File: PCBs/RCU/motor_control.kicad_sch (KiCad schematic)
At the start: 18 parts, among them J300 Right_Encoder_Conn_01x04, J301 Right_Motor_Screw_Terminal_01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, J302 Left_Encoder_Conn_01x04, J303 Left_Motor_Screw_Terminal_01x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, U300 OPA365xxD, U301 DRV8876, U302 OPA365xxD, U303 DRV8876

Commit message: Corrected C302 and C305 values in motor drive units, should be 22nF, not 22uF
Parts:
- C302, C305: value 22uF -> (none)
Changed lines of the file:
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@@
       (effects (font (size 1.27 1.27)) (justify left))
     )
-    (property "Value" "22uF" (id 1) (at 180.34 63.5 0)
+    (property "Value" "" (id 1) (at 180.34 63.5 0)
       (effects (font (size 1.27 1.27)) (justify left))
     )
@@
       (effects (font (size 1.27 1.27)) (justify left))
     )
-    (property "Value" "22uF" (id 1) (at 179.07 118.11 0)
+    (property "Value" "" (id 1) (at 179.07 118.11 0)
       (effects (font (size 1.27 1.27)) (justify left))
     )

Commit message: Added 6V adjustable regulator to power motors and encoders
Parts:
- C302, C305: value (none) -> 22nF
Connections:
- net +9V is gone; now on net +6V: C300.1, C301.1, C303.1, C304.1, U301.11 (VM), U303.11 (VM)
- net +5V renamed +6V

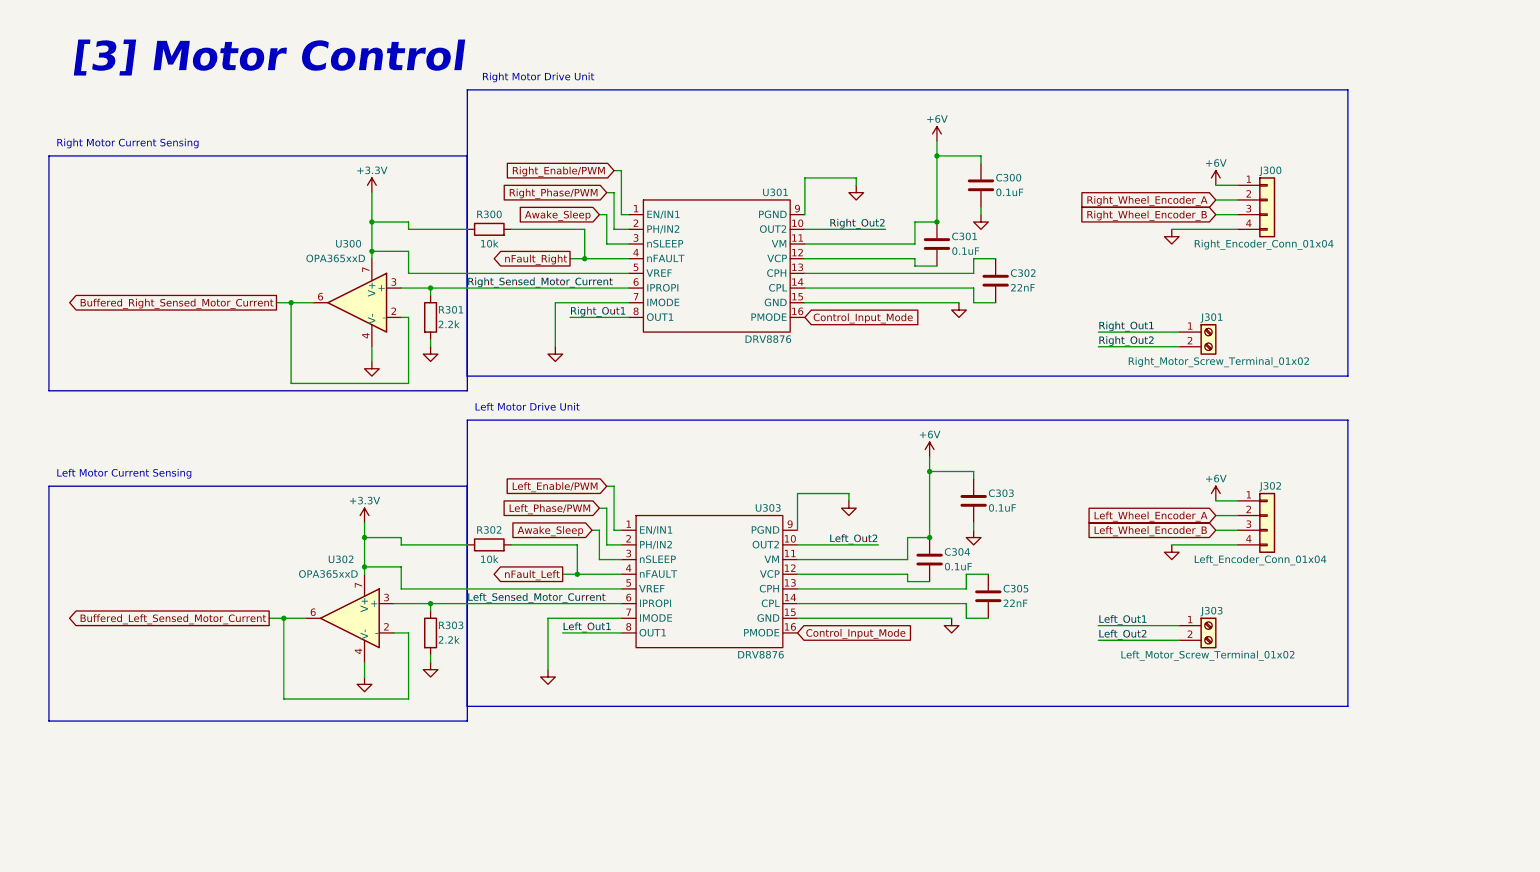
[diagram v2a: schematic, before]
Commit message: scaled down encoder output from 6V to 4V
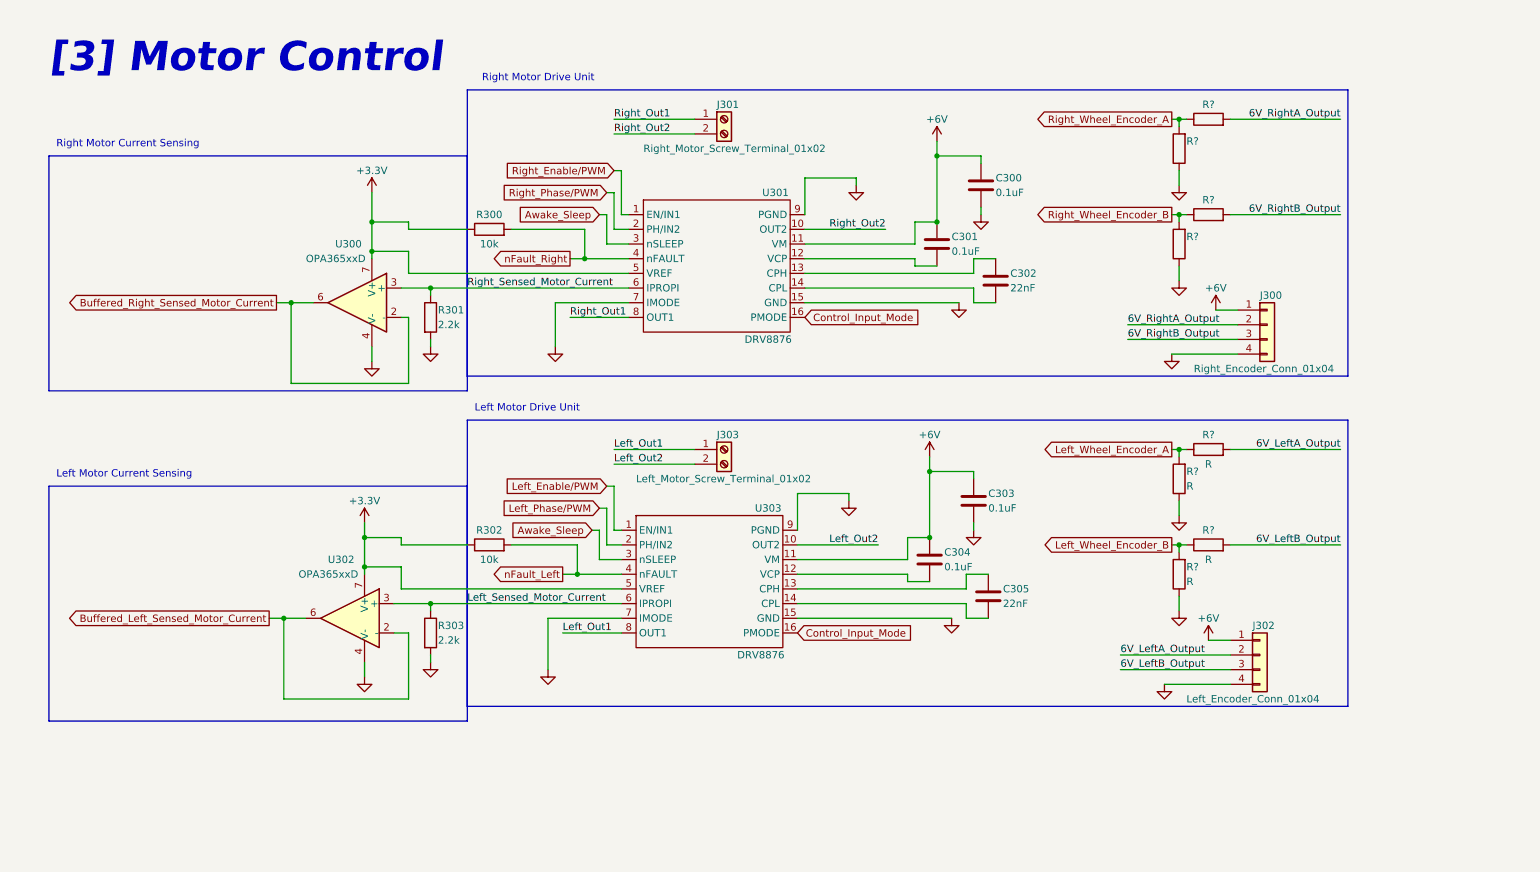
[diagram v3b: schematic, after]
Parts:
- added R? (x4): (no value), symbol Device:R
- added R? (x4): R, symbol Device:R
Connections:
- net GND: now also R?.1, R?.1, R?.1, R?.1
- net Left_Wheel_Encoder_A: now also R?.1, R?.2; no longer J302.2 (Pin_2)
- net Left_Wheel_Encoder_B: now also R?.1, R?.2; no longer J302.3 (Pin_3)
- net Right_Wheel_Encoder_A: now also R?.1, R?.2; no longer J300.2 (Pin_2)
- net Right_Wheel_Encoder_B: now also R?.1, R?.2; no longer J300.3 (Pin_3)
- new net 6V_LeftA_Output: J302.2 (Pin_2), R?.2
- new net 6V_LeftB_Output: J302.3 (Pin_3), R?.2
- new net 6V_RightA_Output: J300.2 (Pin_2), R?.2
- new net 6V_RightB_Output: J300.3 (Pin_3), R?.2
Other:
- moved on the sheet: J300, J301, J302, J303

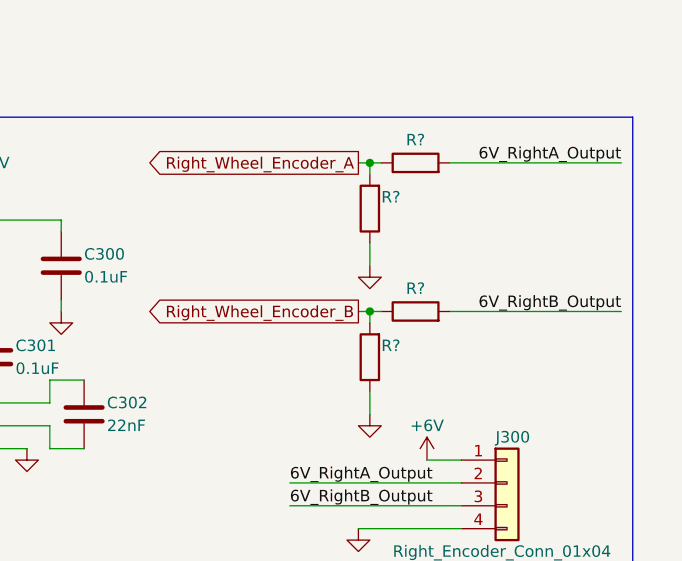
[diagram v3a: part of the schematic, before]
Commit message: Replaced Bidrectional TVS diodes with USBLC-2SC6 unidirectional ESD protection
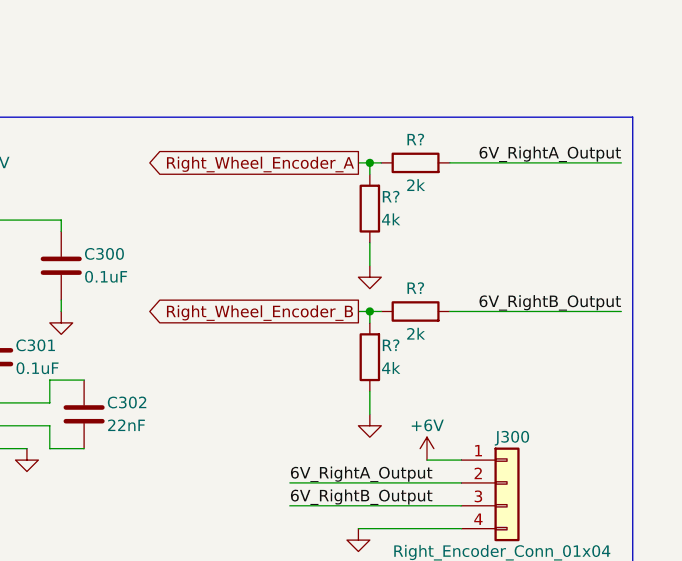
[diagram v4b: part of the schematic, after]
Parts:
- R? (x2): value (none) -> 4k
- R? (x2): value (none) -> 2k
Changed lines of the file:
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@@
       (effects (font (size 1.27 1.27)) (justify right))
     )
-    (property "Value" "" (id 1) (at 210.82 57.15 0)
+    (property "Value" "4k" (id 1) (at 210.82 57.15 0)
       (effects (font (size 1.27 1.27)) (justify right))
     )
@@
       (effects (font (size 1.27 1.27)) (justify right))
     )
-    (property "Value" "" (id 1) (at 210.82 40.64 0)
+    (property "Value" "4k" (id 1) (at 210.82 40.64 0)
       (effects (font (size 1.27 1.27)) (justify right))
     )
@@
     (in_bom yes) (on_board yes)
     (property "Reference" "R?" (id 0) (at 214.63 48.26 90))
-    (property "Value" "" (id 1) (at 214.63 53.34 90))
+    (property "Value" "2k" (id 1) (at 214.63 53.34 90))
     (property "Footprint" "" (id 2) (at 214.63 52.578 90)
       (effects (font (size 1.27 1.27)) hide)
@@
     (in_bom yes) (on_board yes)
     (property "Reference" "R?" (id 0) (at 214.63 31.75 90))
-    (property "Value" "" (id 1) (at 214.63 36.83 90))
+    (property "Value" "2k" (id 1) (at 214.63 36.83 90))
     (property "Footprint" "" (id 2) (at 214.63 36.068 90)
       (effects (font (size 1.27 1.27)) hide)

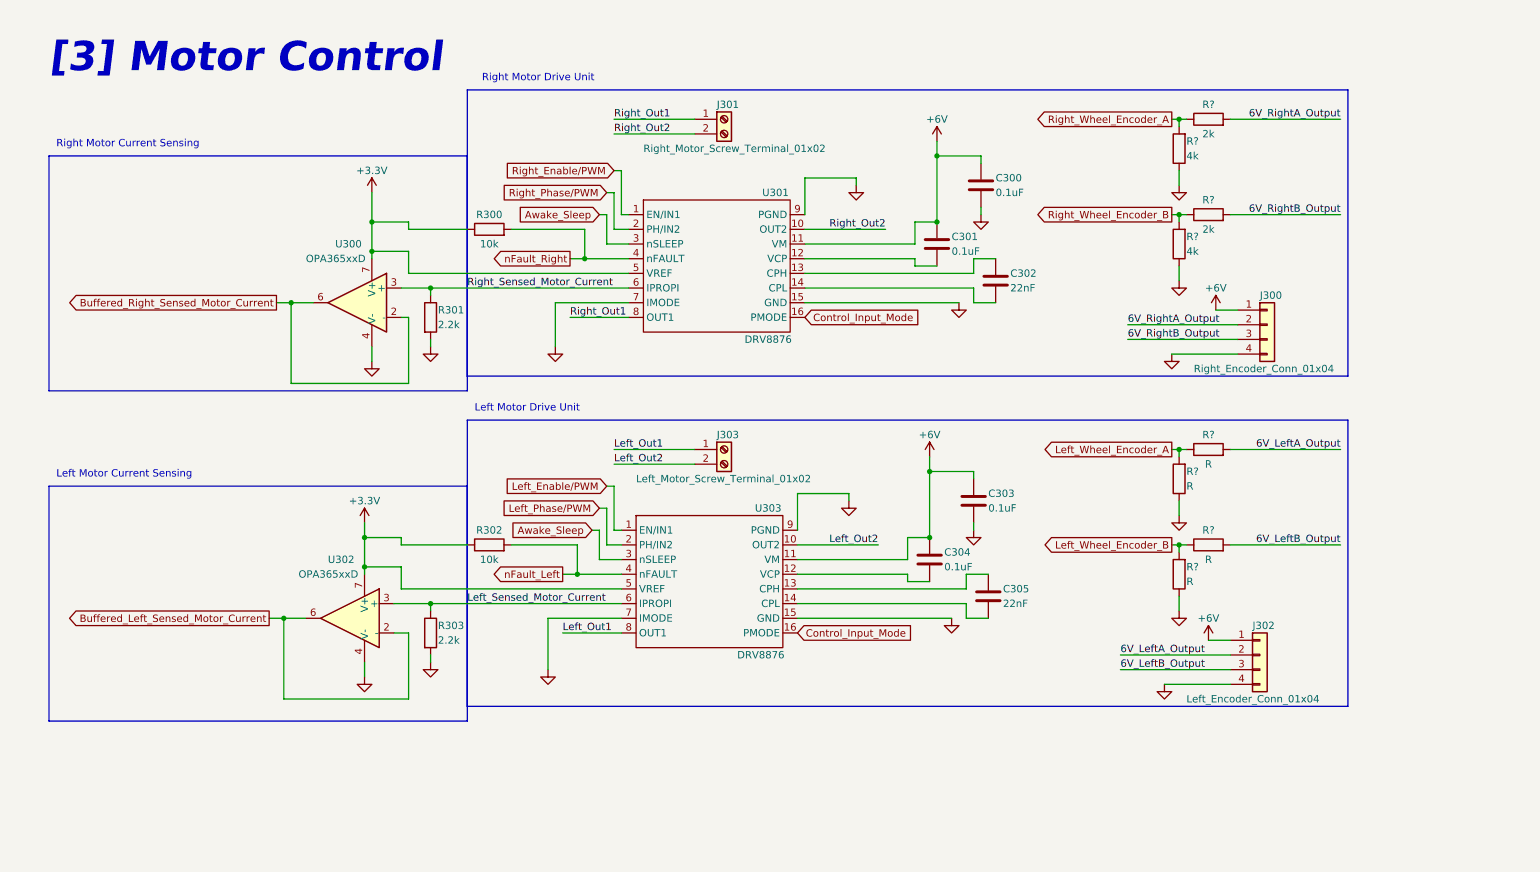
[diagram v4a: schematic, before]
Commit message: Added ESD protection to 3.3V pin of SWD connector, and made motor sheet larger
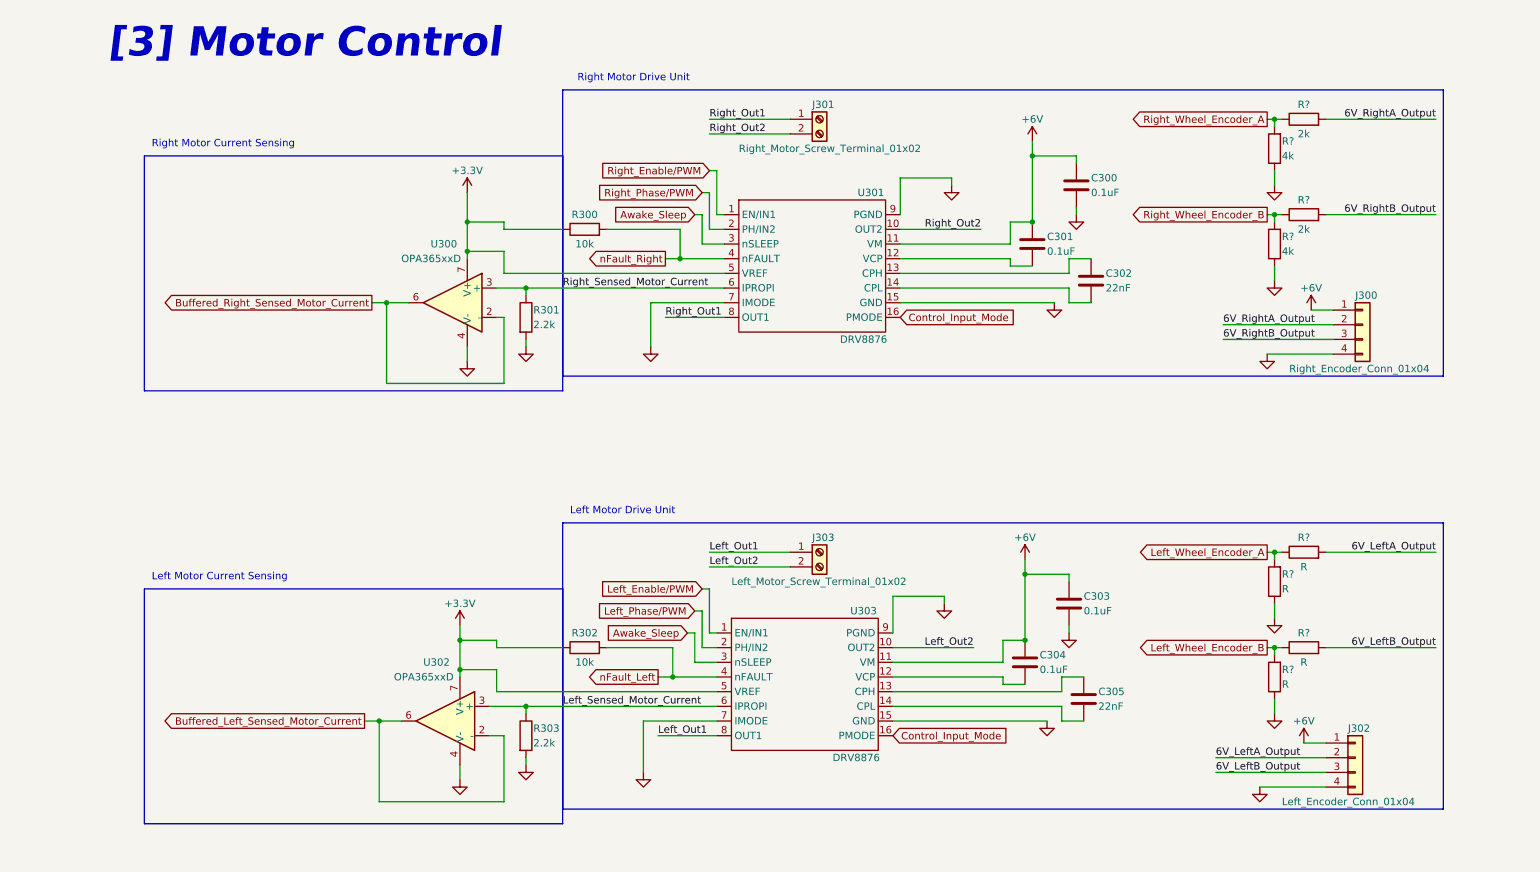
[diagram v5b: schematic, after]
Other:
- moved on the sheet: C300, C301, C302, C303, C304, C305, J300, J301, J302, J303, R300, R301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

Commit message: Add add bidirectional ESD/TVS diodes to encoder and motor terminals
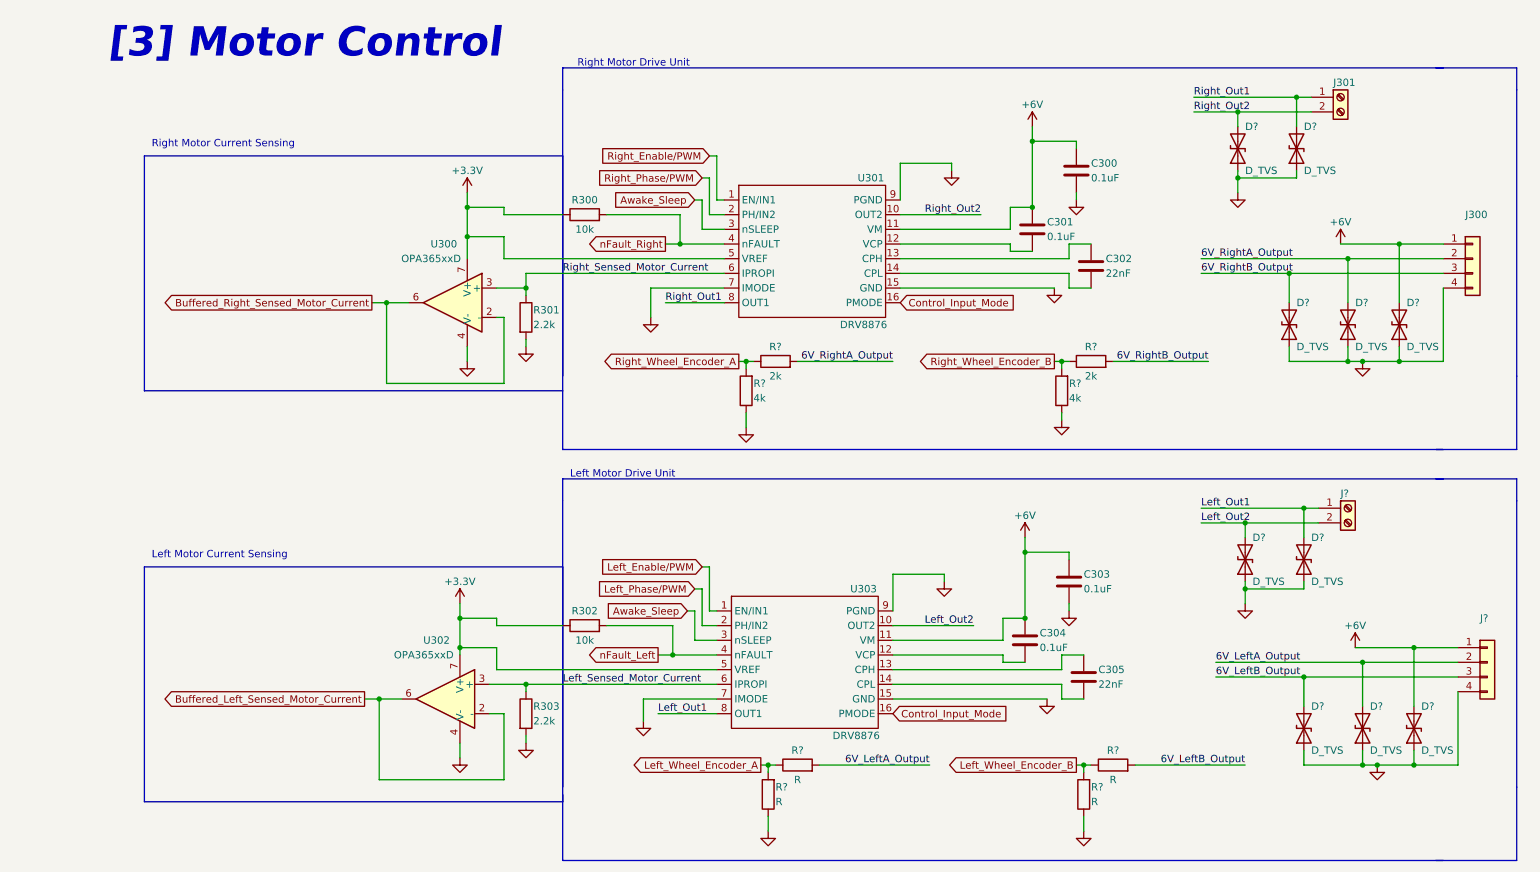
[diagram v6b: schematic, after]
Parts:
- removed J302: Left_Encoder_Conn_01x04, symbol Connector_Generic:Conn_01x04
- removed J303: Left_Motor_Screw_Terminal_01x02, symbol Connector:Screw_Terminal_01x02
- added D? (x10): D_TVS, symbol Device:D_TVS
- added J?: (no value), symbol Connector:Screw_Terminal_01x02
- added J?: (no value), symbol Connector_Generic:Conn_01x04
- J300: value Right_Encoder_Conn_01x04 -> (none)
- J301: value Right_Motor_Screw_Terminal_01x02 -> (none)
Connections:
- net +6V: now also D?.2 (A2), D?.2 (A2), J?.1 (Pin_1)
- net 6V_LeftA_Output: now also D?.2 (A2), J?.2 (Pin_2)
- net 6V_LeftB_Output: now also D?.2 (A2), J?.3 (Pin_3)
- net 6V_RightA_Output: now also D?.2 (A2)
- net 6V_RightB_Output: now also D?.2 (A2)
- net GND: now also D?.1 (A1), D?.1 (A1), D?.1 (A1), D?.1 (A1), D?.1 (A1), D?.1 (A1), D?.1 (A1), D?.1 (A1), D?.1 (A1), D?.1 (A1), J?.4 (Pin_4)
- net Left_Out1: now also D?.2 (A2), J?.1 (Pin_1)
- net Left_Out2: now also D?.2 (A2), J?.2 (Pin_2)
- net Right_Out1: now also D?.2 (A2)
- net Right_Out2: now also D?.2 (A2)
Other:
- moved on the sheet: C300, C301, C302, C303, C304, C305, J300, J301, R300, R302, R303, R?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
